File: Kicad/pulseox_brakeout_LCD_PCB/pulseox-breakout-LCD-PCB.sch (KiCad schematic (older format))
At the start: 20 parts, among them CON3 P3, P1 Header 8, P2 Header 2

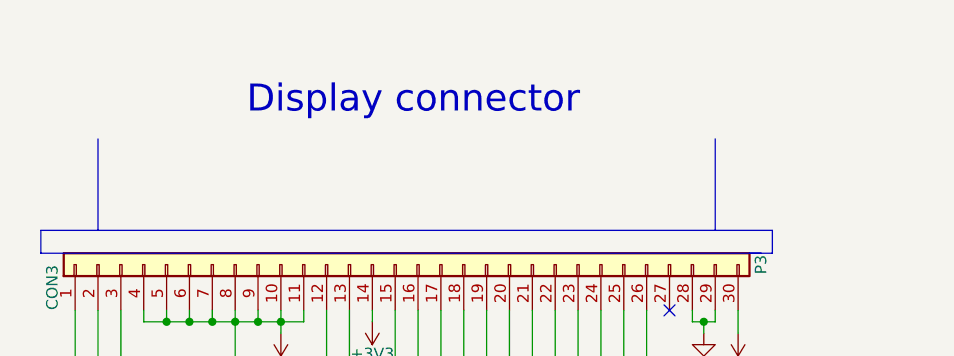
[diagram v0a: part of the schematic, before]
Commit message: Added output PDF files from Kicad project
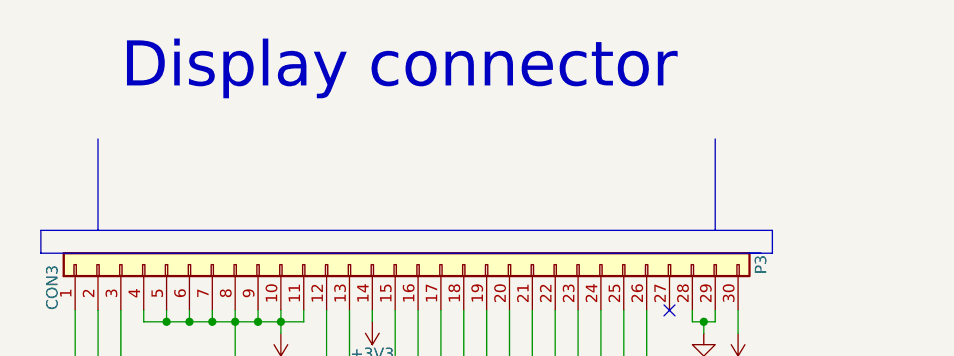
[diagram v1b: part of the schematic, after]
